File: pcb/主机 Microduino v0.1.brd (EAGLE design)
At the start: 45.7 x 46.7 mm, 13 parts, among them IC1 ASM1117, IC2 ASM1117, J1 DCJ0202

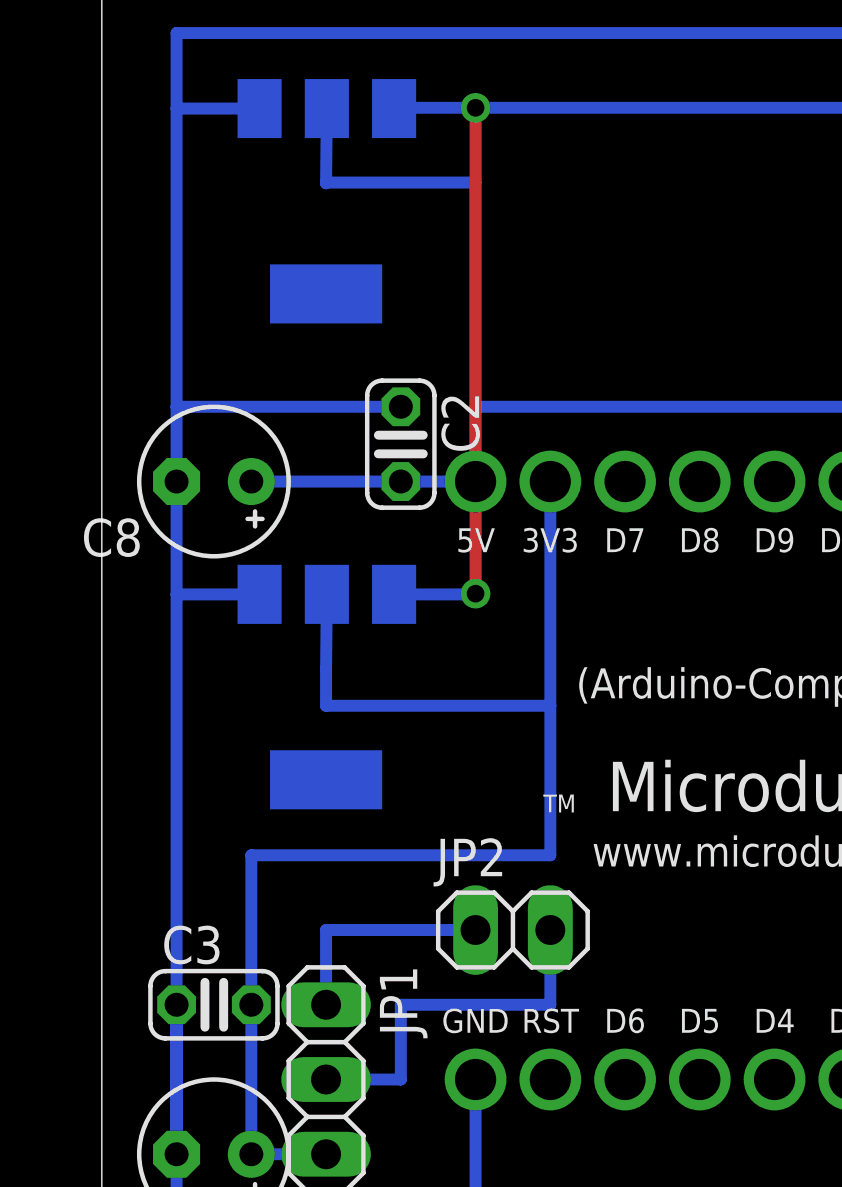
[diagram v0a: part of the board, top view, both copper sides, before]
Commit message: 更新了Microduino面包版PCB
更新了Microduino面包版PCB
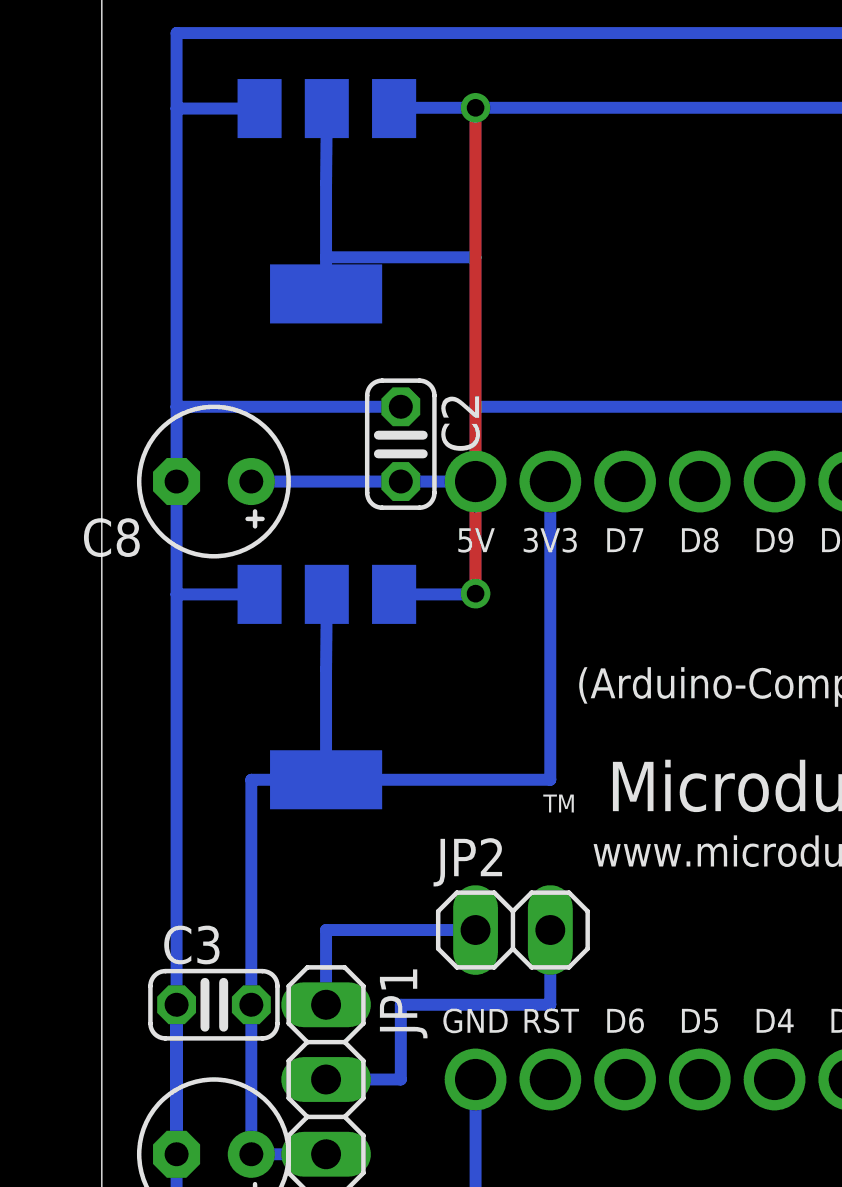
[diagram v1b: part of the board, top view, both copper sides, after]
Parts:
- IC1, IC2: device burr-brown:SOT223 -> MY3:SOT223
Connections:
- net V3.3: now also IC2.4
- net V5.0: now also IC1.4
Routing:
- net V3.3: track 47.0 -> 41.9 mm
- net V5.0: track 53.4 -> 54.6 mm
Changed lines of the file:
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@@
 <elements>
 <element name="U$1" library="MY2" package="PIN-MICRODUINO-1009" value="PING-MICRDUINO-DZ/1009" x="30.48" y="27.94" rot="MR180"/>
-<element name="IC1" library="burr-brown" package="SOT223" value="ASM1117" x="25.4" y="47.625" rot="MR180">
+<element name="IC1" library="MY3" package="SOT223" value="ASM1117" x="25.4" y="47.625" rot="MR180">
 <attribute name="OC_NEWARK" value="14P6981" x="57.15" y="76.835" size="1.778" layer="28" rot="MR180" display="off"/>
 <attribute name="MPN" value="REG1117" x="57.15" y="76.835" size="1.778" layer="28" rot="MR180" display="off"/>
@@
 <element name="R8" library="MY" package="AXIAL-0.3" value="49.9" x="57.15" y="40.64" rot="MR180"/>
 <element name="JP1" library="pinhead" package="1X04" value="" x="25.4" y="16.51" rot="R270"/>
-<element name="IC2" library="burr-brown" package="SOT223" value="ASM1117" x="25.4" y="31.115" rot="MR180">
+<element name="IC2" library="MY3" package="SOT223" value="ASM1117" x="25.4" y="31.115" rot="MR180">
 <attribute name="OC_NEWARK" value="14P6981" x="16.51" y="17.145" size="1.778" layer="28" rot="MR180" display="off"/>
 <attribute name="MPN" value="REG1117" x="16.51" y="17.145" size="1.778" layer="28" rot="MR180" display="off"/>
@@
 <wire x1="55.88" y1="40.64" x2="53.34" y2="40.64" width="0.4064" layer="16"/>
 <wire x1="25.4254" y1="50.7746" x2="25.4" y2="48.2346" width="0.4064" layer="16"/>
-<wire x1="25.4" y1="48.2346" x2="25.4" y2="48.26" width="0.4064" layer="16"/>
-<wire x1="25.4" y1="48.26" x2="30.48" y2="48.26" width="0.4064" layer="16"/>
-<wire x1="30.48" y1="48.26" x2="30.48" y2="40.64" width="0.4064" layer="16"/>
+<wire x1="25.4" y1="45.72" x2="30.48" y2="45.72" width="0.4064" layer="16"/>
+<wire x1="30.48" y1="45.72" x2="30.48" y2="40.64" width="0.4064" layer="16"/>
 <wire x1="22.86" y1="38.1" x2="27.94" y2="38.1" width="0.4064" layer="16"/>
 <wire x1="27.94" y1="38.1" x2="30.48" y2="38.1" width="0.4064" layer="16"/>
+<contactref element="IC1" pad="4"/>
+<wire x1="25.4" y1="44.4754" x2="25.4" y2="45.72" width="0.4064" layer="16"/>
+<wire x1="25.4" y1="45.72" x2="25.4" y2="48.2346" width="0.4064" layer="16"/>
 </signal>
 <signal name="VIN">
@@
 <contactref element="U$1" pad="2"/>
 <wire x1="25.4" y1="15.24" x2="22.86" y2="15.24" width="0.4064" layer="16"/>
-<wire x1="33.02" y1="25.4" x2="33.02" y2="30.48" width="0.4064" layer="16"/>
-<wire x1="33.02" y1="30.48" x2="33.02" y2="38.1" width="0.4064" layer="16"/>
+<wire x1="33.02" y1="27.9654" x2="33.02" y2="38.1" width="0.4064" layer="16"/>
 <wire x1="25.4254" y1="34.2646" x2="25.4" y2="31.7246" width="0.4064" layer="16"/>
-<wire x1="25.4" y1="31.7246" x2="25.4" y2="30.48" width="0.4064" layer="16"/>
-<wire x1="25.4" y1="30.48" x2="33.02" y2="30.48" width="0.4064" layer="16"/>
 <wire x1="22.86" y1="15.24" x2="22.86" y2="20.32" width="0.4064" layer="16"/>
-<wire x1="33.02" y1="25.4" x2="22.86" y2="25.4" width="0.4064" layer="16"/>
-<wire x1="22.86" y1="25.4" x2="22.86" y2="20.32" width="0.4064" layer="16"/>
+<wire x1="22.86" y1="27.9654" x2="22.86" y2="20.32" width="0.4064" layer="16"/>
+<contactref element="IC2" pad="4"/>
+<wire x1="25.4" y1="27.9654" x2="33.02" y2="27.9654" width="0.4064" layer="16"/>
+<wire x1="22.86" y1="27.9654" x2="25.4" y2="27.9654" width="0.4064" layer="16"/>
+<wire x1="25.4" y1="31.7246" x2="25.4" y2="27.9654" width="0.4064" layer="16"/>
 </signal>
 <signal name="RESET">
